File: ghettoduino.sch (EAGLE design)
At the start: 13 parts

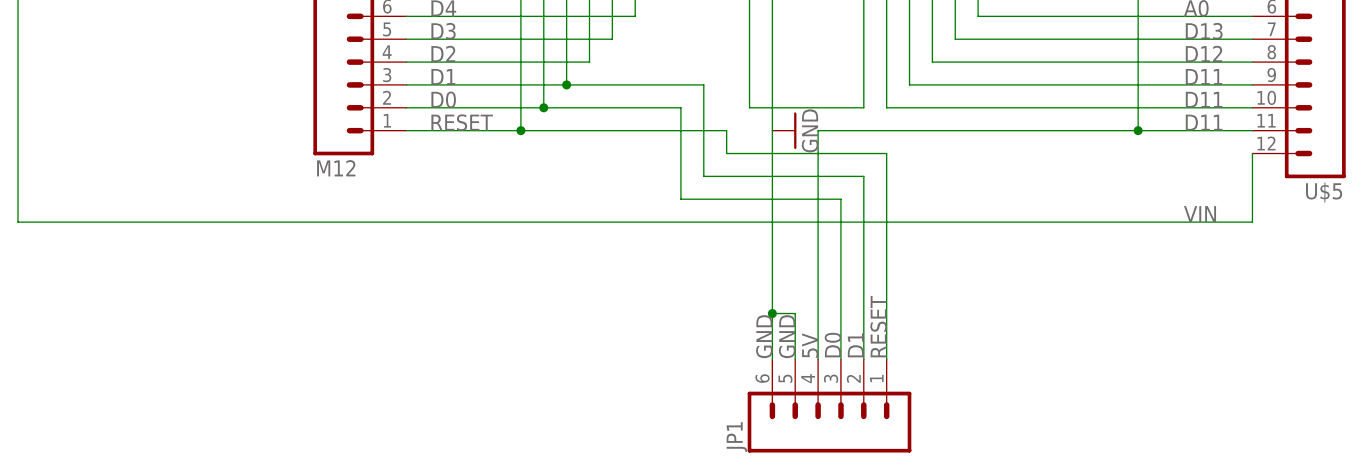
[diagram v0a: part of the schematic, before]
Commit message: Added p-channel MOSFET for reverse power protection.
Gerber, eps files still need update.
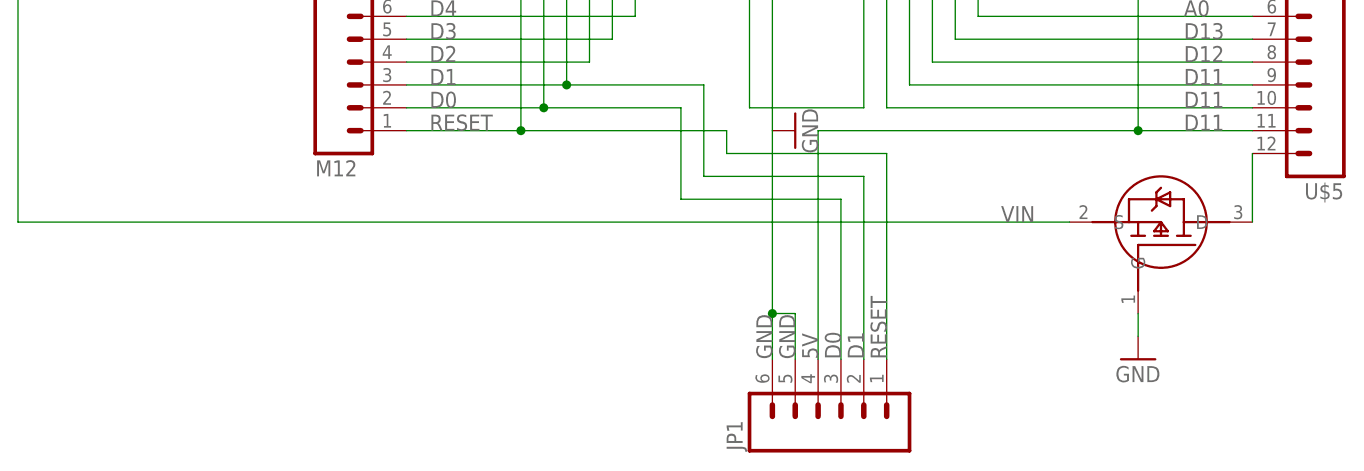
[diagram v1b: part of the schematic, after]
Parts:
- added U$3: P-MOSFET-PMV48XP, 1dah:P-MOSFET-PMV48XP
- 5V: value ZLDO1117 -> 5V-LDO-ZLDO1117; device 1dah:ZLDO1117 -> 1dah:5V-LDO-ZLDO1117
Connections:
- new net N$1: U$3.D, U$5.12
- net GND: now also U$3.G
- net VIN: now also U$3.S; no longer U$5.12
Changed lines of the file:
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@@
 <layer number="29" name="tStop" color="7" fill="3" visible="no" active="no"/>
 <layer number="30" name="bStop" color="7" fill="6" visible="no" active="no"/>
-<layer number="31" name="tCream" color="7" fill="4" visible="no" active="no"/>
-<layer number="32" name="bCream" color="7" fill="5" visible="no" active="no"/>
+<layer number="31" name="tCream" color="12" fill="4" visible="no" active="no"/>
+<layer number="32" name="bCream" color="12" fill="5" visible="no" active="no"/>
 <layer number="33" name="tFinish" color="6" fill="3" visible="no" active="no"/>
 <layer number="34" name="bFinish" color="6" fill="6" visible="no" active="no"/>
@@
 <layer number="46" name="Milling" color="3" fill="1" visible="no" active="no"/>
 <layer number="47" name="Measures" color="7" fill="1" visible="no" active="no"/>
-<layer number="48" name="Document" color="7" fill="1" visible="no" active="no"/>
+<layer number="48" name="Document" color="14" fill="1" visible="no" active="no"/>
 <layer number="49" name="Reference" color="7" fill="1" visible="no" active="no"/>
 <layer number="50" name="dxf" color="7" fill="1" visible="no" active="no"/>
@@
 <part name="GND8" library="SparkFun" deviceset="GND" device=""/>
 <part name="GND9" library="SparkFun" deviceset="GND" device=""/>
-<part name="5V" library="1dah" deviceset="ZLDO1117" device=""/>
+<part name="5V" library="1dah" deviceset="5V-LDO" device="-ZLDO1117"/>
 <part name="U$2" library="1dah" deviceset="M12" device="LOCK" value="M12"/>
 <part name="C3" library="1dah" deviceset="CAP" device="0603-CAP" value="18pF"/>
@@
 <part name="JP1" library="1dah" deviceset="M06" device="LOCK"/>
 <part name="U$5" library="1dah" deviceset="M12" device="LOCK" value="M12"/>
+<part name="U$3" library="1dah" deviceset="P-MOSFET" device="-PMV48XP"/>
+<part name="GND10" library="SparkFun" deviceset="GND" device=""/>
 </parts>
 <sheets>
@@
 <instance part="JP1" gate="G$1" x="5.08" y="-88.9" rot="R90"/>
 <instance part="U$5" gate="G$1" x="60.96" y="-48.26" rot="R180"/>
+<instance part="U$3" gate="G$1" x="40.64" y="-68.58" rot="MR90"/>
+<instance part="GND10" gate="1" x="38.1" y="-83.82"/>
 </instances>
 <busses>
@@
 <pinref part="5V" gate="G$1" pin="GND"/>
 </segment>
+<segment>
+<pinref part="U$3" gate="G$1" pin="G"/>
+<pinref part="GND10" gate="1" pin="GND"/>
+<wire x1="38.1" y1="-81.28" x2="38.1" y2="-78.74" width="0.1524" layer="91"/>
+</segment>
 </net>
 <net name="VIN" class="0">
 <segment>
-<wire x1="50.8" y1="-68.58" x2="50.8" y2="-60.96" width="0.1524" layer="91"/>
-<wire x1="-86.36" y1="-68.58" x2="50.8" y2="-68.58" width="0.1524" layer="91"/>
+<wire x1="-86.36" y1="-68.58" x2="30.48" y2="-68.58" width="0.1524" layer="91"/>
 <wire x1="0" y1="76.2" x2="-86.36" y2="76.2" width="0.1524" layer="91"/>
 <wire x1="-86.36" y1="76.2" x2="-86.36" y2="-68.58" width="0.1524" layer="91"/>
@@
 <wire x1="0" y1="71.12" x2="0" y2="76.2" width="0.1524" layer="91"/>
 <junction x="0" y="71.12"/>
-<label x="43.18" y="-68.58" size="1.778" layer="95"/>
+<label x="22.86" y="-68.58" size="1.778" layer="95"/>
 <label x="-10.16" y="76.2" size="1.778" layer="95"/>
 <pinref part="5V" gate="G$1" pin="VIN"/>
 <pinref part="C8" gate="G$1" pin="1"/>
-<pinref part="U$5" gate="G$1" pin="12"/>
+<pinref part="U$3" gate="G$1" pin="S"/>
 </segment>
 </net>
@@
 </segment>
 </net>
+<net name="N$1" class="0">
+<segment>
+<pinref part="U$3" gate="G$1" pin="D"/>
+<pinref part="U$5" gate="G$1" pin="12"/>
+<wire x1="50.8" y1="-68.58" x2="50.8" y2="-60.96" width="0.1524" layer="91"/>
+</segment>
+</net>

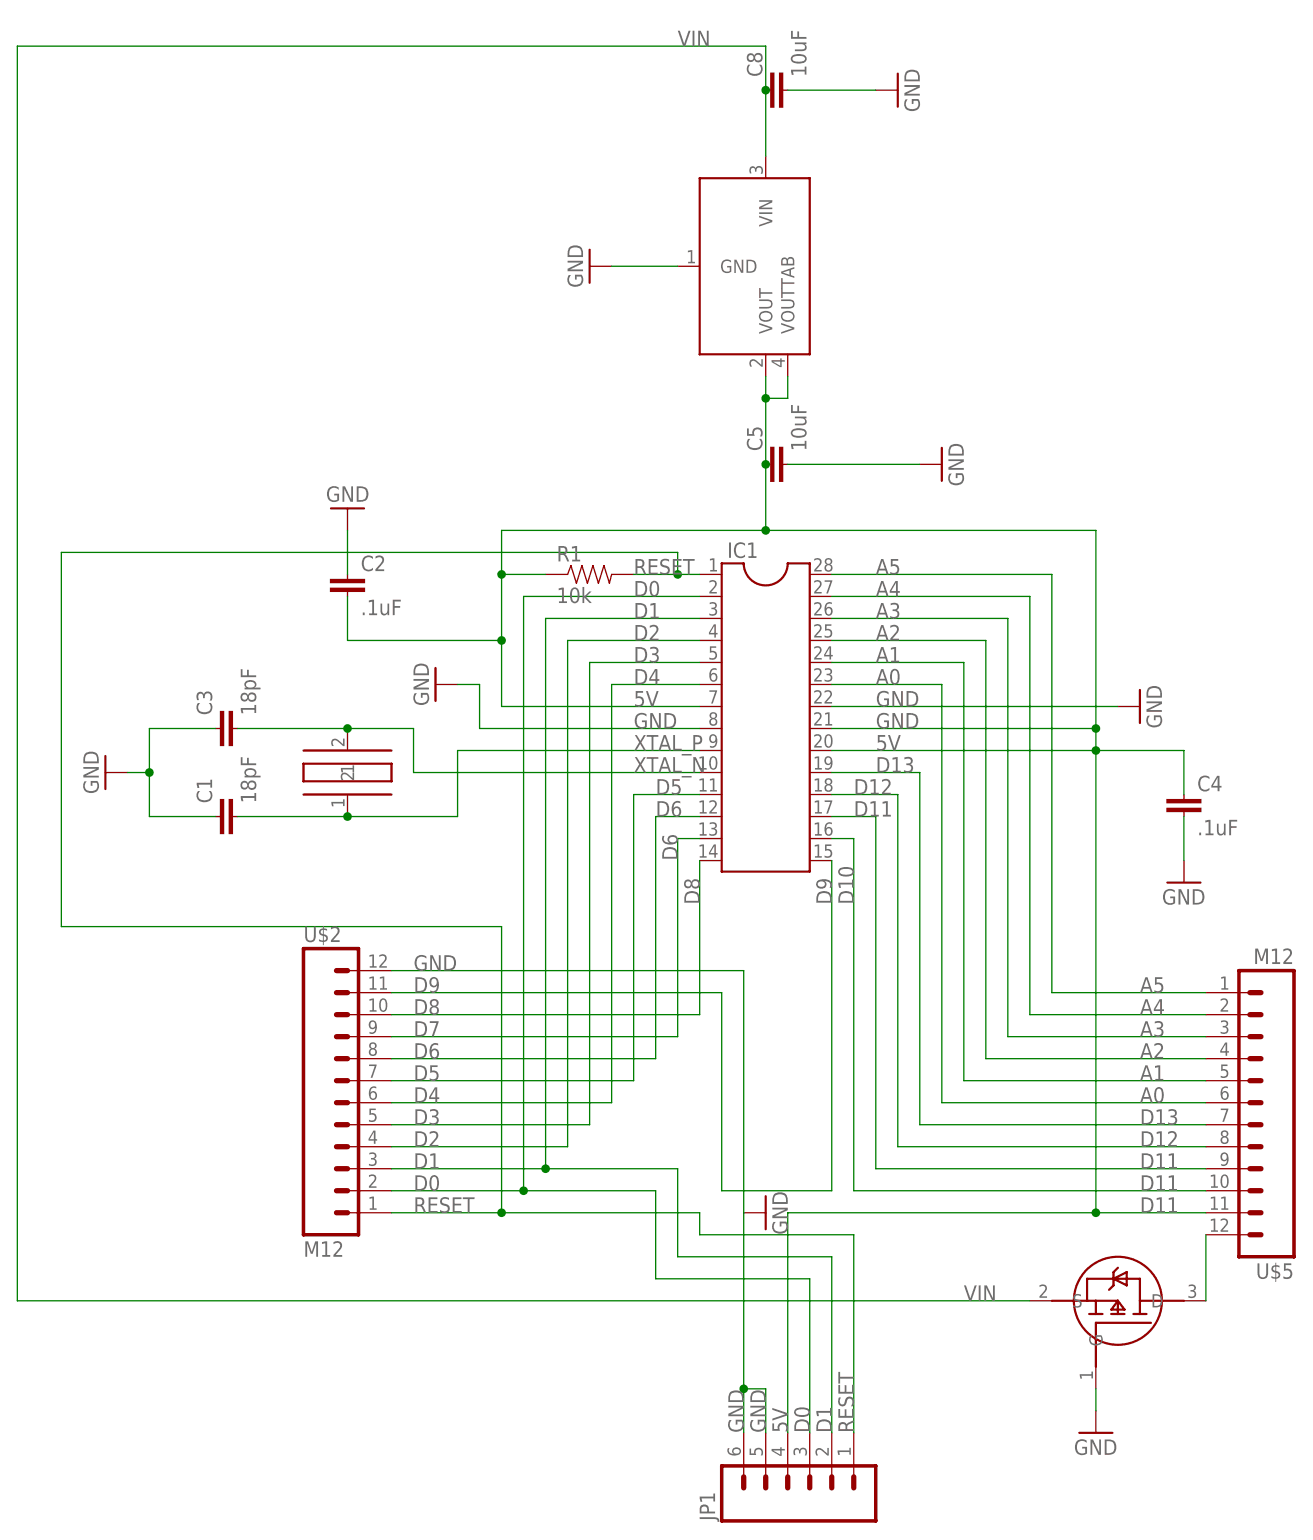
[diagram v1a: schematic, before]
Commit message: Added p-FET reverse bias protection, more markings, extra ground pin, general re-arranging and cleanup.
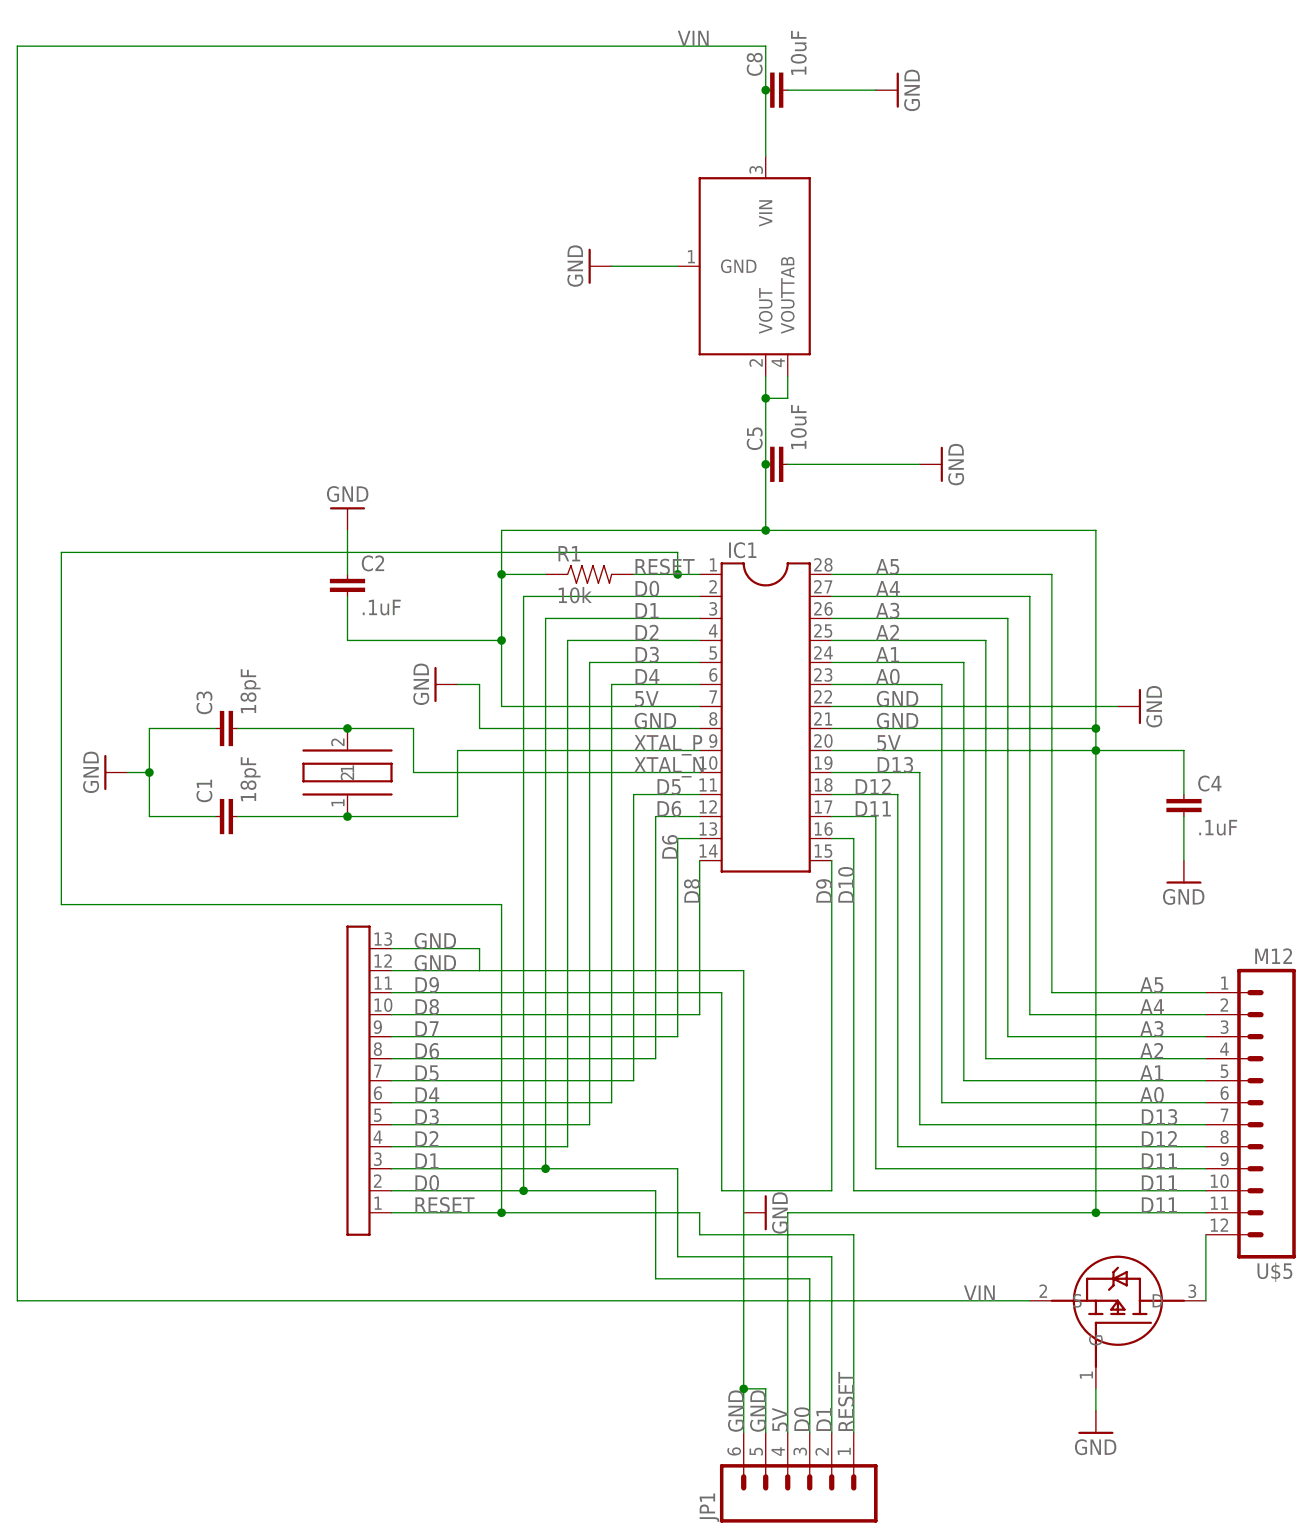
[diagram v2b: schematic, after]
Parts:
- U$2: device 1dah:M12LOCK -> 1dah:M13
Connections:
- net GND: now also U$2.13
